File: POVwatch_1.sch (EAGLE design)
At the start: 49 parts, among them Q1 S8050, U1 ATMEGA168P-QFN32, U2 ADXL345, U3 MCP6001-SOT23, U4 APDS-9008, U5 TP4055, U6 3.3V, U7 CH340E, Y1 7.3728MHz

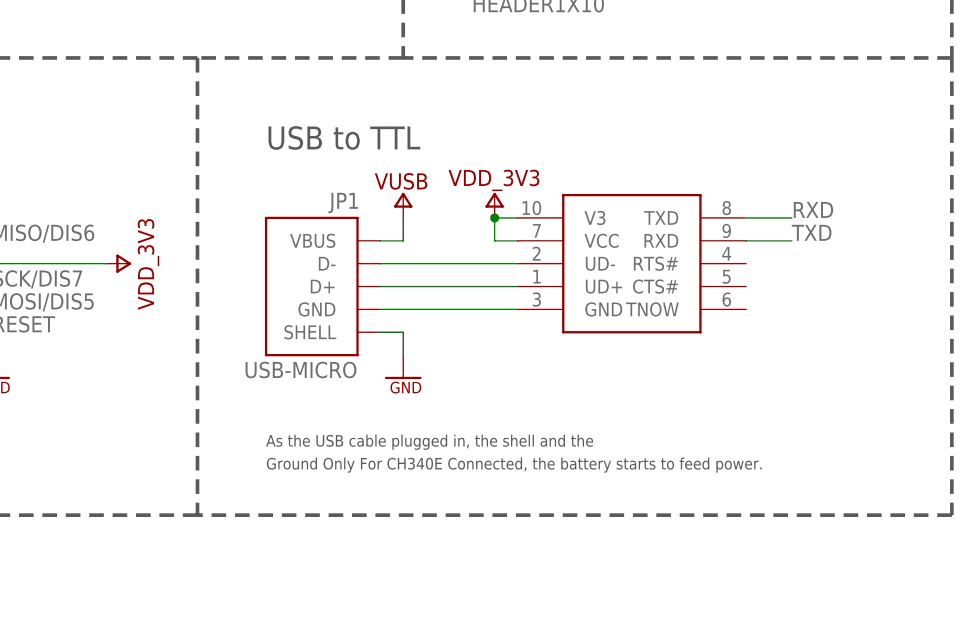
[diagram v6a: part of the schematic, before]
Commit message: Fixed CH340E ground connection
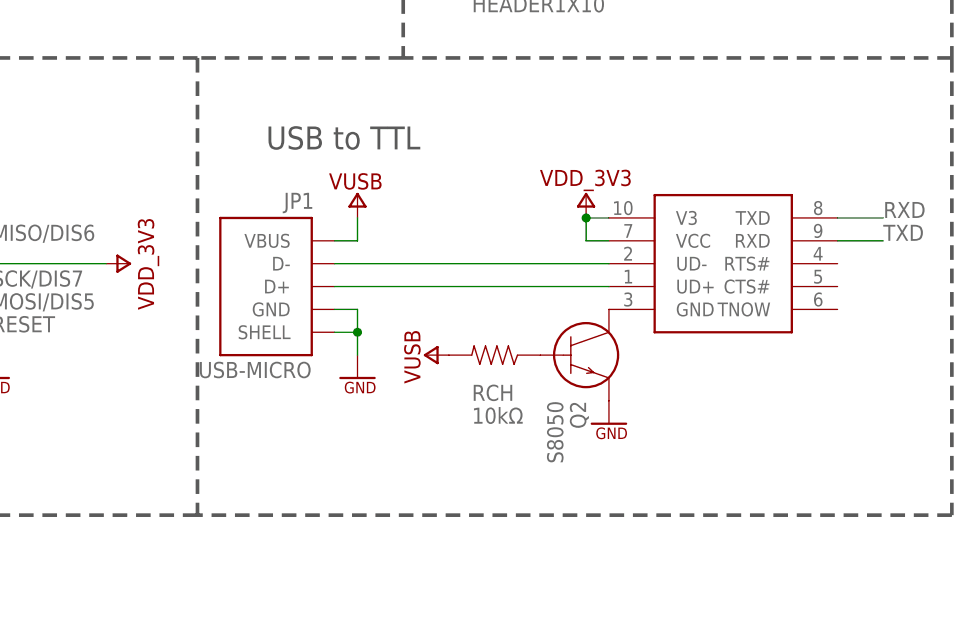
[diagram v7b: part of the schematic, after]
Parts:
- added Q2: S8050, MyLibrary:NPN-0
- added RCH: 10kΩ, MyLibrary:RES-0603
- Q1: device MyLibrary:NPN-SOT23 -> MyLibrary:NPN-0
- U6: device MyLibrary:XC6206-SOT23 -> MyLibrary:XC6206-0
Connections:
- new net TRIGND: Q2.B, RCH.1
- net GND: now also JP1.GND, Q2.E
- net GND(CH340E): now also Q2.C; no longer JP1.GND
- net VUSB: now also RCH.2
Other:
- note removed: "As the USB cable plugged in, the shell and the"
- note removed: "Ground Only For CH340E Connected, the battery starts to feed power."
- moved on the sheet: JP1
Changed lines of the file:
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@@
 <part name="DP2" library="MyLibrary" deviceset="LED" device="-1206" value="GREEN"/>
 <part name="SUPPLY1" library="MyLibrary" deviceset="VDD_3V3" device=""/>
-<part name="Q1" library="MyLibrary" deviceset="NPN" device="-SOT23" value="S8050"/>
+<part name="Q1" library="MyLibrary" deviceset="NPN" device="-0" value="S8050"/>
 <part name="U3" library="MyLibrary" deviceset="MCP6001" device="-SOT23"/>
 <part name="U4" library="MyLibrary" deviceset="APDS-9008" device=""/>
@@
 <part name="RTRIG" library="MyLibrary" deviceset="RES" device="-0603" value="1kΩ"/>
 <part name="SUPPLY28" library="MyLibrary" deviceset="GND" device=""/>
-<part name="U6" library="MyLibrary" deviceset="XC6206" device="-SOT23" value="3.3V"/>
+<part name="U6" library="MyLibrary" deviceset="XC6206" device="-0" value="3.3V"/>
 <part name="SUPPLY29" library="MyLibrary" deviceset="GND" device=""/>
 <part name="CVOUT" library="MyLibrary" deviceset="CAP" device="-0603" value="1μF"/>
@@
 <part name="FB3" library="MyLibrary" deviceset="BROAD-STICK" device=""/>
 <part name="FB4" library="MyLibrary" deviceset="BROAD-STICK" device=""/>
+<part name="Q2" library="MyLibrary" deviceset="NPN" device="-0" value="S8050"/>
+<part name="SUPPLY27" library="MyLibrary" deviceset="GND" device=""/>
+<part name="SUPPLY30" library="MyLibrary" deviceset="VUSB" device=""/>
+<part name="RCH" library="MyLibrary" deviceset="RES" device="-0603" value="10kΩ"/>
 </parts>
 <sheets>
@@
 <text x="-134.62" y="7.62" size="1.27" layer="97" font="vector">Enable internal pull-up resistors </text>
 <text x="-134.62" y="5.08" size="1.27" layer="97" font="vector">in AVR to avoid adding RSDA and RSCL.</text>
-<text x="167.64" y="-35.56" size="1.27" layer="97" font="vector">As the USB cable plugged in, the shell and the </text>
-<text x="167.64" y="-38.1" size="1.27" layer="97" font="vector">Ground Only For CH340E Connected, the battery starts to feed power.</text>
 <text x="167.64" y="-2.54" size="2.54" layer="97" font="vector">USB to TTL</text>
 <wire x1="160.02" y1="7.62" x2="160.02" y2="-43.18" width="0.4064" layer="97" style="longdash"/>
@@
 <instance part="SUPPLY13" gate="GND" x="50.8" y="35.56"/>
 <instance part="U5" gate="P" x="93.98" y="35.56"/>
-<instance part="JP1" gate="A" x="175.26" y="-17.78" rot="MR0"/>
+<instance part="JP1" gate="A" x="170.18" y="-17.78" rot="MR0"/>
 <instance part="Y1" gate="A" x="-38.1" y="15.24"/>
-<instance part="U7" gate="G$1" x="208.28" y="-15.24"/>
+<instance part="U7" gate="G$1" x="218.44" y="-15.24"/>
 <instance part="SUPPLY16" gate="VUSB" x="71.12" y="43.18"/>
-<instance part="SUPPLY18" gate="GND" x="182.88" y="-27.94"/>
-<instance part="SUPPLY19" gate="VUSB" x="182.88" y="-7.62"/>
-<instance part="SUPPLY23" gate="VDD_3V3" x="193.04" y="-7.62"/>
+<instance part="SUPPLY18" gate="GND" x="177.8" y="-27.94"/>
+<instance part="SUPPLY19" gate="VUSB" x="177.8" y="-7.62"/>
+<instance part="SUPPLY23" gate="VDD_3V3" x="203.2" y="-7.62"/>
 <instance part="RESET" gate="A" x="-50.8" y="20.32" rot="R90"/>
 <instance part="SUPPLY24" gate="GND" x="-50.8" y="12.7"/>
@@
 <instance part="FB3" gate="A" x="35.56" y="-63.5"/>
 <instance part="FB4" gate="A" x="35.56" y="-71.12"/>
+<instance part="Q2" gate="A" x="203.2" y="-25.4" rot="MR90"/>
+<instance part="SUPPLY27" gate="GND" x="205.74" y="-33.02"/>
+<instance part="SUPPLY30" gate="VUSB" x="185.42" y="-25.4" rot="R90"/>
+<instance part="RCH" gate="A" x="193.04" y="-25.4" smashed="yes">
+<attribute name="NAME" x="190.5" y="-30.48" size="1.778" layer="95"/>
+<attribute name="VALUE" x="190.5" y="-33.02" size="1.778" layer="96"/>
+</instance>
 </instances>
 <busses>
@@
 <segment>
 <pinref part="U7" gate="G$1" pin="V3"/>
-<wire x1="195.58" y1="-10.16" x2="193.04" y2="-10.16" width="0.1524" layer="91"/>
-<wire x1="193.04" y1="-10.16" x2="193.04" y2="-12.7" width="0.1524" layer="91"/>
+<wire x1="205.74" y1="-10.16" x2="203.2" y2="-10.16" width="0.1524" layer="91"/>
+<wire x1="203.2" y1="-10.16" x2="203.2" y2="-12.7" width="0.1524" layer="91"/>
 <pinref part="U7" gate="G$1" pin="VCC"/>
-<wire x1="193.04" y1="-12.7" x2="195.58" y2="-12.7" width="0.1524" layer="91"/>
+<wire x1="203.2" y1="-12.7" x2="205.74" y2="-12.7" width="0.1524" layer="91"/>
 <pinref part="SUPPLY23" gate="VDD_3V3" pin="VDD_3V3"/>
-<junction x="193.04" y="-10.16"/>
+<junction x="203.2" y="-10.16"/>
 </segment>
 <segment>
@@
 <pinref part="JP1" gate="A" pin="SHELL"/>
 <pinref part="SUPPLY18" gate="GND" pin="GND"/>
-<wire x1="180.34" y1="-22.86" x2="182.88" y2="-22.86" width="0.1524" layer="91"/>
-<wire x1="182.88" y1="-22.86" x2="182.88" y2="-25.4" width="0.1524" layer="91"/>
+<wire x1="175.26" y1="-22.86" x2="177.8" y2="-22.86" width="0.1524" layer="91"/>
+<wire x1="177.8" y1="-22.86" x2="177.8" y2="-25.4" width="0.1524" layer="91"/>
+<pinref part="JP1" gate="A" pin="GND"/>
+<wire x1="175.26" y1="-20.32" x2="177.8" y2="-20.32" width="0.1524" layer="91"/>
+<wire x1="177.8" y1="-20.32" x2="177.8" y2="-22.86" width="0.1524" layer="91"/>
+<junction x="177.8" y="-22.86"/>
 </segment>
 <segment>
@@
 <junction x="25.4" y="-71.12"/>
 </segment>
+<segment>
+<pinref part="Q2" gate="A" pin="E"/>
+<pinref part="SUPPLY27" gate="GND" pin="GND"/>
+</segment>
 </net>
 <net name="SCL" class="0">
@@
 <segment>
 <pinref part="U7" gate="G$1" pin="TXD"/>
-<wire x1="220.98" y1="-10.16" x2="226.06" y2="-10.16" width="0.1524" layer="91"/>
-<label x="226.06" y="-10.16" size="1.778" layer="95" font="vector"/>
+<wire x1="231.14" y1="-10.16" x2="236.22" y2="-10.16" width="0.1524" layer="91"/>
+<label x="236.22" y="-10.16" size="1.778" layer="95" font="vector"/>
 </segment>
 </net>
@@
 <segment>
 <pinref part="U7" gate="G$1" pin="RXD"/>
-<wire x1="220.98" y1="-12.7" x2="226.06" y2="-12.7" width="0.1524" layer="91"/>
-<label x="226.06" y="-12.7" size="1.778" layer="95" font="vector"/>
+<wire x1="231.14" y1="-12.7" x2="236.22" y2="-12.7" width="0.1524" layer="91"/>
+<label x="236.22" y="-12.7" size="1.778" layer="95" font="vector"/>
 </segment>
 </net>
@@
 <pinref part="JP1" gate="A" pin="VBUS"/>
 <pinref part="SUPPLY19" gate="VUSB" pin="VUSB"/>
-<wire x1="180.34" y1="-12.7" x2="182.88" y2="-12.7" width="0.1524" layer="91"/>
-<wire x1="182.88" y1="-12.7" x2="182.88" y2="-10.16" width="0.1524" layer="91"/>
+<wire x1="175.26" y1="-12.7" x2="177.8" y2="-12.7" width="0.1524" layer="91"/>
+<wire x1="177.8" y1="-12.7" x2="177.8" y2="-10.16" width="0.1524" layer="91"/>
+</segment>
+<segment>
+<pinref part="RCH" gate="A" pin="2"/>
+<pinref part="SUPPLY30" gate="VUSB" pin="VUSB"/>
 </segment>
 </net>
@@
 <segment>
 <pinref part="JP1" gate="A" pin="D-"/>
-<wire x1="180.34" y1="-15.24" x2="195.58" y2="-15.24" width="0.1524" layer="91"/>
+<wire x1="175.26" y1="-15.24" x2="205.74" y2="-15.24" width="0.1524" layer="91"/>
 <pinref part="U7" gate="G$1" pin="UD-"/>
 </segment>
@@
 <pinref part="JP1" gate="A" pin="D+"/>
 <pinref part="U7" gate="G$1" pin="UD+"/>
-<wire x1="180.34" y1="-17.78" x2="195.58" y2="-17.78" width="0.1524" layer="91"/>
-</segment>
-</net>
-<net name="GND(CH340E)" class="0">
-<segment>
-<pinref part="JP1" gate="A" pin="GND"/>
-<pinref part="U7" gate="G$1" pin="GND"/>
-<wire x1="180.34" y1="-20.32" x2="195.58" y2="-20.32" width="0.1524" layer="91"/>
+<wire x1="175.26" y1="-17.78" x2="205.74" y2="-17.78" width="0.1524" layer="91"/>
 </segment>
 </net>
@@
 </segment>
 </net>
+<net name="GND(CH340E)" class="0">
+<segment>
+<pinref part="U7" gate="G$1" pin="GND"/>
+<pinref part="Q2" gate="A" pin="C"/>
+</segment>
+</net>
+<net name="TRIGND" class="0">
+<segment>
+<pinref part="Q2" gate="A" pin="B"/>
+<pinref part="RCH" gate="A" pin="1"/>
+</segment>
+</net>
